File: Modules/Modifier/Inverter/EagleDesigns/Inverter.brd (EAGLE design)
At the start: 100 x 80 mm, 6 parts, among them U1 TINY85-20-DIP

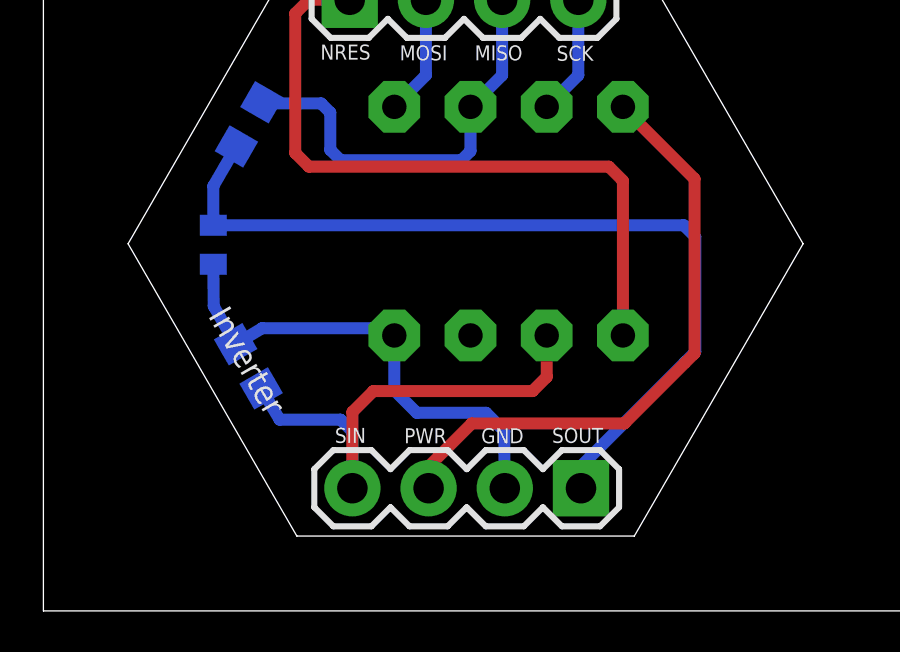
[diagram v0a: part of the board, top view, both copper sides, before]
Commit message: changed 0403 cap to 0603 SMD cap
to solder without difficulty!
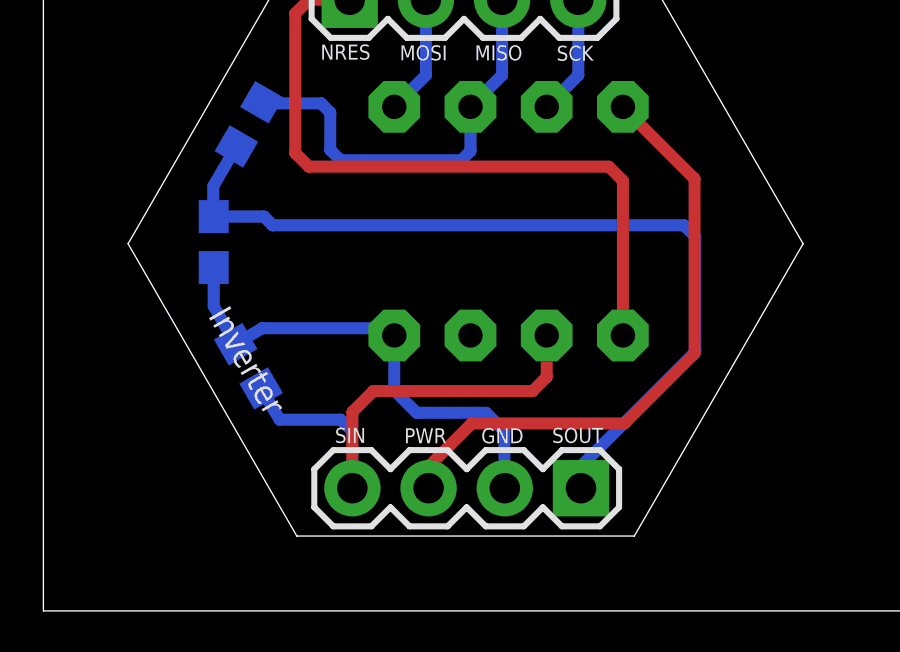
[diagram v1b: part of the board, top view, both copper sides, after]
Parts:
- C1: device adafruit:C0402 -> adafruit:C0603
- moved C1 0.09 mm to (5.68, 12.3), turned to 270 degrees
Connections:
- net 1X3SOUT: now also C1.1; no longer C1.2
- net GND: now also C1.2; no longer C1.1
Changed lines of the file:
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@@
 <attribute name="VALUE" x="8.529596875" y="17.2775375" size="0.6" layer="28" rot="MR30"/>
 </element>
-<element name="C1" library="adafruit" package="C0402" value="0.22uF" x="5.6642" y="12.2047" smashed="yes" rot="MR90">
-<attribute name="VALUE" x="4.318" y="10.8712" size="0.6" layer="28" rot="MR90"/>
-</element>
+<element name="C1" library="adafruit" package="C0603" value="0.22uF" x="5.6769" y="12.2936" rot="MR270"/>
 </elements>
 <signals>
@@
 <contactref element="U1" pad="4"/>
 <contactref element="R1" pad="1"/>
-<contactref element="C1" pad="1"/>
 <wire x1="6.4076" y1="8.88951875" x2="5.6769" y2="10.16" width="0.4" layer="16"/>
-<wire x1="5.6769" y1="10.16" x2="5.6642" y2="11.5547" width="0.4" layer="16"/>
 <wire x1="6.4076" y1="8.88951875" x2="7.2898" y2="9.4234" width="0.4" layer="16"/>
 <wire x1="7.2898" y1="9.4234" x2="11.4554" y2="9.4234" width="0.4" layer="16"/>
@@
 <wire x1="15.367" y1="5.9944" x2="15.367" y2="4.1021" width="0.4" layer="16"/>
 <wire x1="15.367" y1="4.1021" x2="15.3797" y2="4.0894" width="0.4" layer="16"/>
+<contactref element="C1" pad="2"/>
+<wire x1="5.6769" y1="11.4436" x2="5.6769" y2="10.16" width="0.4064" layer="16"/>
 </signal>
 <signal name="1X3SOUT">
 <contactref element="JP1" pad="1"/>
 <contactref element="R2" pad="1"/>
-<contactref element="C1" pad="2"/>
 <wire x1="6.433" y1="15.481778125" x2="5.6642" y2="14.1605" width="0.4" layer="16"/>
-<wire x1="5.6642" y1="14.1605" x2="5.6642" y2="12.8547" width="0.4" layer="16"/>
 <wire x1="17.9197" y1="4.0894" x2="17.9197" y2="4.826" width="0.4" layer="16"/>
-<wire x1="17.9197" y1="4.826" x2="21.3741" y2="8.2804" width="0.4" layer="16"/>
-<wire x1="21.3741" y1="8.2804" x2="21.7043" y2="8.6106" width="0.4" layer="16"/>
-<wire x1="5.6642" y1="12.8547" x2="21.3464" y2="12.8547" width="0.4" layer="16"/>
+<wire x1="17.9197" y1="4.826" x2="21.7297" y2="8.636" width="0.4" layer="16"/>
 <wire x1="21.3464" y1="12.8547" x2="21.7297" y2="12.4714" width="0.4" layer="16"/>
 <wire x1="21.7297" y1="12.4714" x2="21.7297" y2="8.636" width="0.4" layer="16"/>
-<wire x1="21.7297" y1="8.636" x2="21.7043" y2="8.6106" width="0.4" layer="16"/>
+<contactref element="C1" pad="1"/>
+<wire x1="5.6642" y1="14.1605" x2="5.6642" y2="13.1563" width="0.4064" layer="16"/>
+<wire x1="5.6642" y1="13.1563" x2="5.6769" y2="13.1436" width="0.4064" layer="16"/>
+<wire x1="21.3464" y1="12.8547" x2="7.6431" y2="12.8547" width="0.4064" layer="16"/>
+<wire x1="7.6431" y1="12.8547" x2="7.3533" y2="13.1445" width="0.4064" layer="16"/>
+<wire x1="7.3533" y1="13.1445" x2="5.6778" y2="13.1445" width="0.4064" layer="16"/>
+<wire x1="5.6778" y1="13.1445" x2="5.6769" y2="13.1436" width="0.4064" layer="16"/>
 </signal>
 <signal name="OUT(MISO)">
